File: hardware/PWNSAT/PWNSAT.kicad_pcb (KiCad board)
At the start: 2 copper layers, 83 x 83 mm, 138 parts, among them J2 Conn_01x04_Pin, J3 Sensors, J4 USB_A, J5 USB_A, J6 Source, SW1 SW_Push, SW2 SW_Push, SW4 USB Selector, U2 W25N02KVZEIR, U3 EA3059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

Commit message: feat(Hw):Route_Updated
Pending review
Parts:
- moved C30 14.6 mm to (54.1, 75.7), turned to -90 degrees
- moved C29 13.7 mm to (55.3, 76.0), turned to -90 degrees
- moved R8 6.63 mm to (63.3, 67.4)
- moved C20 4.78 mm to (74.5, 64.5)
- moved C21 3.68 mm to (78.0, 62.3), turned to -90 degrees
- moved R6 1.38 mm to (74.6, 59.8)
- moved R13 1.05 mm to (65.2, 73.2), turned to -90 degrees
- moved R3 0.84 mm to (56.1, 51.4)
- moved C6 0.84 mm to (56.1, 50.5)
- moved Y1 0.83 mm to (55.5, 57.2)
- moved C19 0.83 mm to (55.4, 59.7)
- moved C14 0.83 mm to (56.1, 52.3)
- moved R4 0.83 mm to (55.8, 53.5)
- moved C22 0.82 mm to (55.5, 54.8)
- moved C13 0.81 mm to (73.6, 56.6)
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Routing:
- net GND: track 93.1 -> 111.4 mm, vias 106 -> 115
- net +3V3: track 240.3 -> 230.7 mm, vias 7 -> 9
- net /Sensor/R1_MOSI: track 35.6 -> 44.8 mm, vias 0 -> 1
- net Net-(U1B-EMMC_CLK/FSPI_CLK/GPIO4_B1_D): track 12.7 -> 3.50 mm, vias 2 -> 0
- net /Sensor/R1_NSS: track 43.4 -> 52.3 mm
- net /Sensor/R1_SCK: track 47.9 -> 55.9 mm
- net /core/VDD_ARM: track 101.9 -> 108.2 mm
- net +1V8: track 183.9 -> 189.8 mm
- net /core/FSPI_SCK: track 4.86 -> 10.2 mm
- net /Sensor/R1_MISO: track 33.1 -> 38.1 mm, vias 0 -> 2
- net Net-(C21-Pad1): track 7.00 -> 3.68 mm
- net /Sensor/INT1: track 29.0 -> 32.1 mm
- net /core/FSPI_D1: track 10.3 -> 13.0 mm, vias 0 -> 2
- net /core/SZQ: track 8.08 -> 5.47 mm, vias 2 -> 0
- net /Sensor/R0_MISO: track 19.4 -> 21.8 mm
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
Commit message: feat(Hw):update_route
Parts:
- removed kibuzzard-6985158A (x2): G***, kibuzzard-6985158A
- added kibuzzard-69B43A9C: G***, kibuzzard-69B43A9C, F.Cu at (30.1, 60.7)
- added kibuzzard-69B43B5E: G***, kibuzzard-69B43B5E, B.Cu at (60.3, 49.2)
- moved C33 1.04 mm to (40.9, 44.6)
- moved R16 1.03 mm to (49.7, 44.6)
- moved R15 1.03 mm to (40.0, 44.6)
- moved R17 1.03 mm to (39.0, 44.6)
- moved C31 1.02 mm to (47.9, 44.6)
- moved R14 1.01 mm to (48.8, 44.6)
- moved R20 0.99 mm to (48.8, 41.7)
- moved R22 0.99 mm to (39.0, 41.7)
- moved R19 0.99 mm to (39.9, 41.7)
- moved C39 0.99 mm to (40.8, 41.7)
- moved R23 0.98 mm to (49.8, 41.7)
- moved C41 0.96 mm to (47.9, 41.7)
- moved Y1 0.47 mm to (55.4, 56.8)
- moved C22 0.45 mm to (55.4, 54.3)
- moved C19 0.43 mm to (55.4, 59.3)
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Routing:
- net +1V8: track 189.8 -> 147.9 mm, vias 12 -> 10
- net GND: track 111.4 -> 123.8 mm, vias 115 -> 137
- net /core/VDD_ARM: track 108.2 -> 101.2 mm, vias 8 -> 7
- net /Sensor/INT1: track 32.1 -> 35.7 mm
- net /Sensor/FSYNC: track 27.3 -> 30.2 mm
- net /Sensor/R0_ANT_SW: track 24.4 -> 27.0 mm
- net +3V3: track 230.7 -> 232.8 mm
- net /Sensor/INT2: track 38.6 -> 36.8 mm
- net +5V: track 210.6 -> 209.1 mm, vias 19 -> 18
- net /core/VCC_DDR: track 83.3 -> 82.0 mm
- net /power_supply/FB1: track 4.51 -> 3.47 mm
- net /power_supply/FB2: track 4.60 -> 3.60 mm
- net /power_supply/FB4: track 4.47 -> 3.51 mm
- net /power_supply/FB3: track 4.62 -> 3.71 mm
- net /core/NPOR: track 73.6 -> 72.9 mm
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
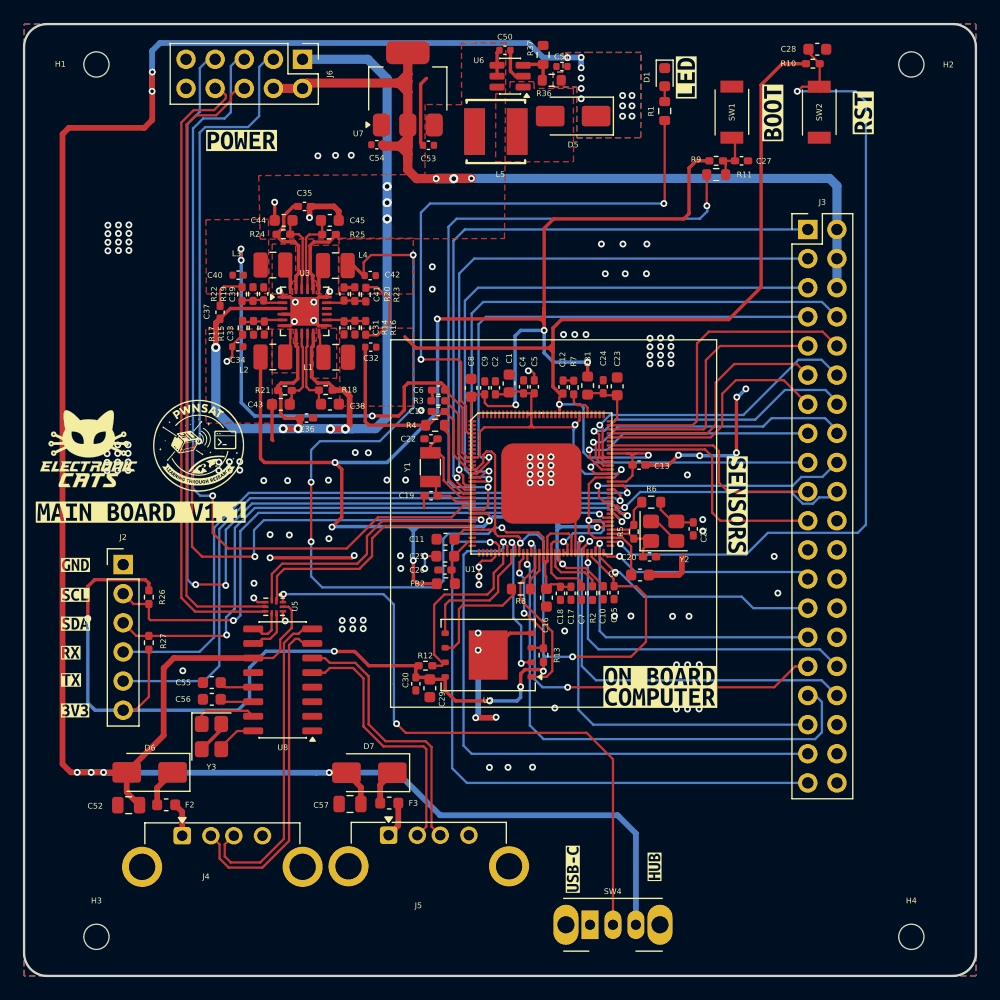
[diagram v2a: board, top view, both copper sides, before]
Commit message: Feat(Hw): Change to 4-layer
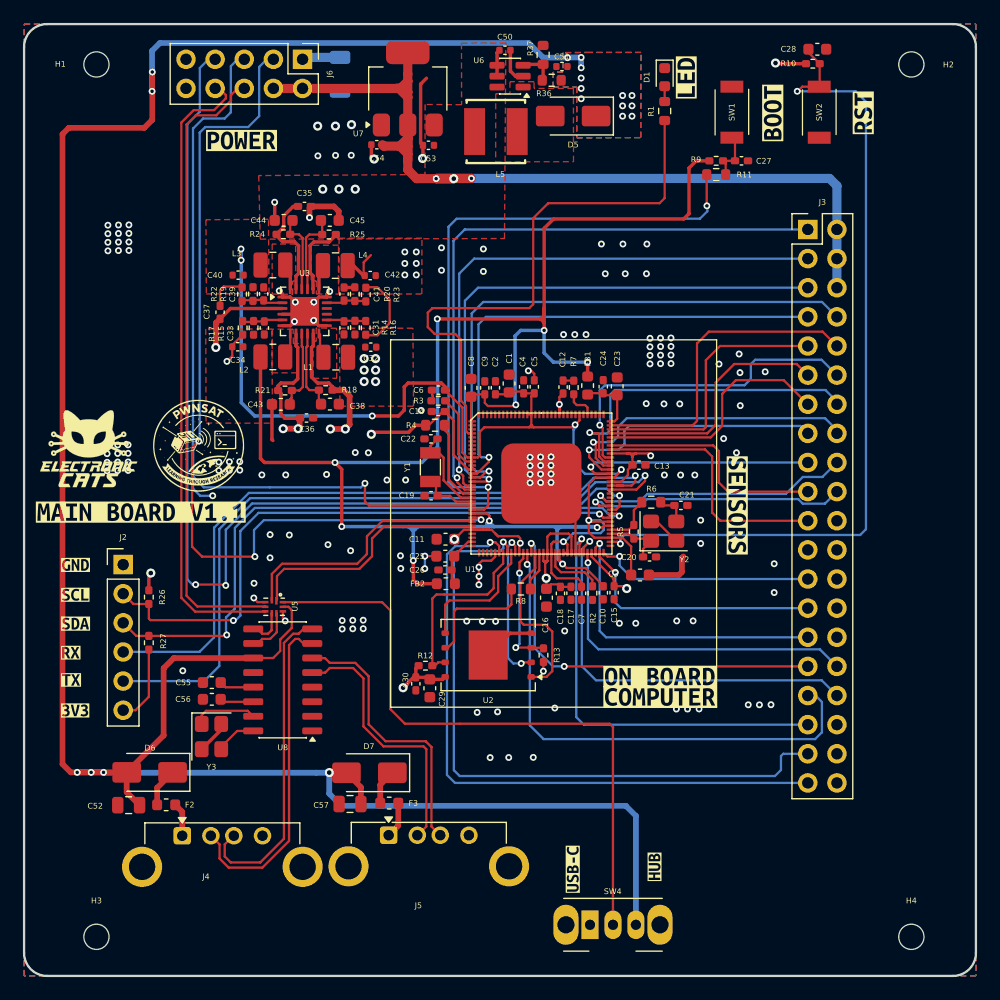
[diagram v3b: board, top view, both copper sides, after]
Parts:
- removed kibuzzard-69B43B5E: G***, kibuzzard-69B43B5E
- added C46: 220uF, Capacitor_SMD:C_1206_3216Metric, B.Cu at (47.5, 22.5)
- added kibuzzard-69B883B0: G***, kibuzzard-69B883B0, B.Cu at (60.3, 49.2)
- moved C21 2.31 mm to (77.2, 60.1), turned to 0 degrees
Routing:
- net +3V3: track 232.8 -> 57.5 mm, vias 9 -> 16
- net /core/VCC_DDR: track 82.0 -> 16.9 mm, vias 4 -> 7
- net VCC: track 113.5 -> 55.5 mm
- net GND: track 123.8 -> 92.6 mm, vias 137 -> 152
- net /Sensor/R1_NSS: track 52.3 -> 57.5 mm
- net /core/DEBUG_TX: track 58.6 -> 63.8 mm
- net +1V8: track 147.9 -> 153.0 mm
- net /Sensor/R1_MISO: track 37.7 -> 34.6 mm
- net /core/DEBUG_RX: track 57.2 -> 60.0 mm
- net /core/LED: track 52.0 -> 49.3 mm, vias 2 -> 0
- net /Sensor/R1_DIO1: track 27.1 -> 29.6 mm
- net /Sensor/R1_DIO2: track 27.1 -> 29.6 mm
- net /Sensor/SCL_SENS: track 21.3 -> 23.5 mm
- net +5V: track 209.1 -> 211.1 mm
- net /Source_Connector/Battery: track 70.8 -> 72.5 mm, vias 1 -> 2
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- added copper zone on In2.Cu, net +3V3
- added copper zone on In2.Cu, net /core/VCC_DDR
- added copper zone on In1.Cu, net GND
- added copper zone on In2.Cu, net VCC
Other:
- copper layers 2 -> 4
